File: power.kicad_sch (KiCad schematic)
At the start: 67 parts, among them J5 S7B-XH-A

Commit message: feat: change B+/P+ to B.Cu and onto one pad
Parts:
- removed PAD2: pad, MyFootLib:INPUT_PAD, symbol MyySym:PAD
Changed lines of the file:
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@@
 	)
 	(junction
-		(at 172.72 24.13)
-		(diameter 0)
-		(color 0 0 0 0)
-	)
-	(junction
 		(at 241.3 29.21)
 		(diameter 0)
@@
 	(wire
 		(pts
-			(xy 172.72 24.13) (xy 185.42 24.13)
-		)
-		(stroke
-			(width 0)
-			(type default)
-		)
-	)
-	(wire
-		(pts
 			(xy 60.96 144.78) (xy 67.31 144.78)
 		)
@@
 	(wire
 		(pts
-			(xy 160.02 24.13) (xy 172.72 24.13)
+			(xy 160.02 24.13) (xy 185.42 24.13)
 		)
 		(stroke
@@
 					(unit 1)
 				)
-			)
-		)
-	)
-	(symbol
-		(lib_id "MyySym:PAD")
-		(at 172.72 24.13 0)
-		(unit 1)
-		(body_style 1)
-		(exclude_from_sim no)
-		(in_bom yes)
-		(on_board yes)
-		(in_pos_files yes)
-		(dnp no)
-		(fields_autoplaced yes)
-		(property "Reference" "PAD2"
-			(at 175.26 22.8599 0)
-			(show_name no)
-			(do_not_autoplace no)
-			(effects
-				(font
-					(size 1.27 1.27)
-				)
-				(justify left)
-			)
-		)
-		(property "Value" "pad"
-			(at 175.26 25.3999 0)
-			(show_name no)
-			(do_not_autoplace no)
-			(effects
-				(font
-					(size 1.27 1.27)
-				)
-				(justify left)
-			)
-		)
-		(property "Footprint" "MyFootLib:INPUT_PAD"
-			(at 177.8 24.13 0)
-			(hide yes)
-			(show_name no)
-			(do_not_autoplace no)
-			(effects
-				(font
-					(size 1.27 1.27)
-				)
-			)
-		)
-		(property "Datasheet" "~"
-			(at 177.8 24.13 0)
-			(hide yes)
-			(show_name no)
-			(do_not_autoplace no)
-			(effects
-				(font
-					(size 1.27 1.27)
-				)
-			)
-		)
-		(property "Description" "PAD"
-			(at 172.72 26.162 0)
-			(hide yes)
-			(show_name no)
-			(do_not_autoplace no)
-			(effects
-				(font
-					(size 1.27 1.27)
-				)
-			)
-		)
-		(pin "1"
-		)
-		(instances
-			(project "stm32f446re-mc33772c"
-				(path "/7455d46c-434c-42dd-9f3f-f89cdb6d3cc2"
-					(reference "PAD2")
-					(unit 1)
-				)

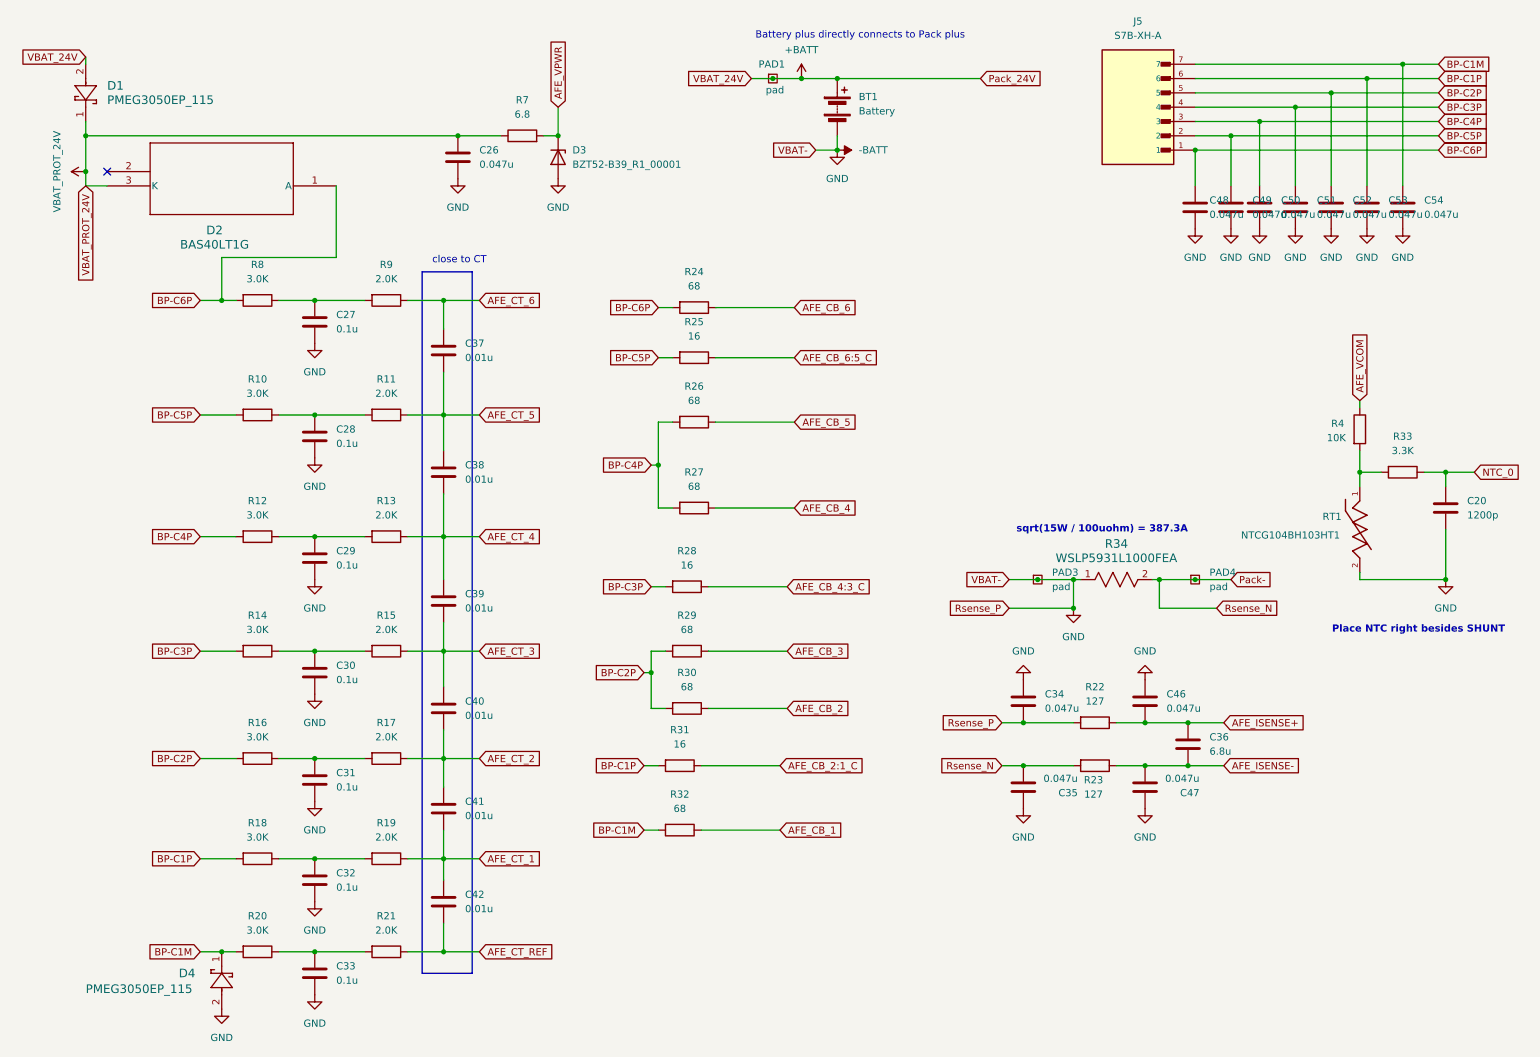
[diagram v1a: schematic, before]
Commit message: add LCPC Part #
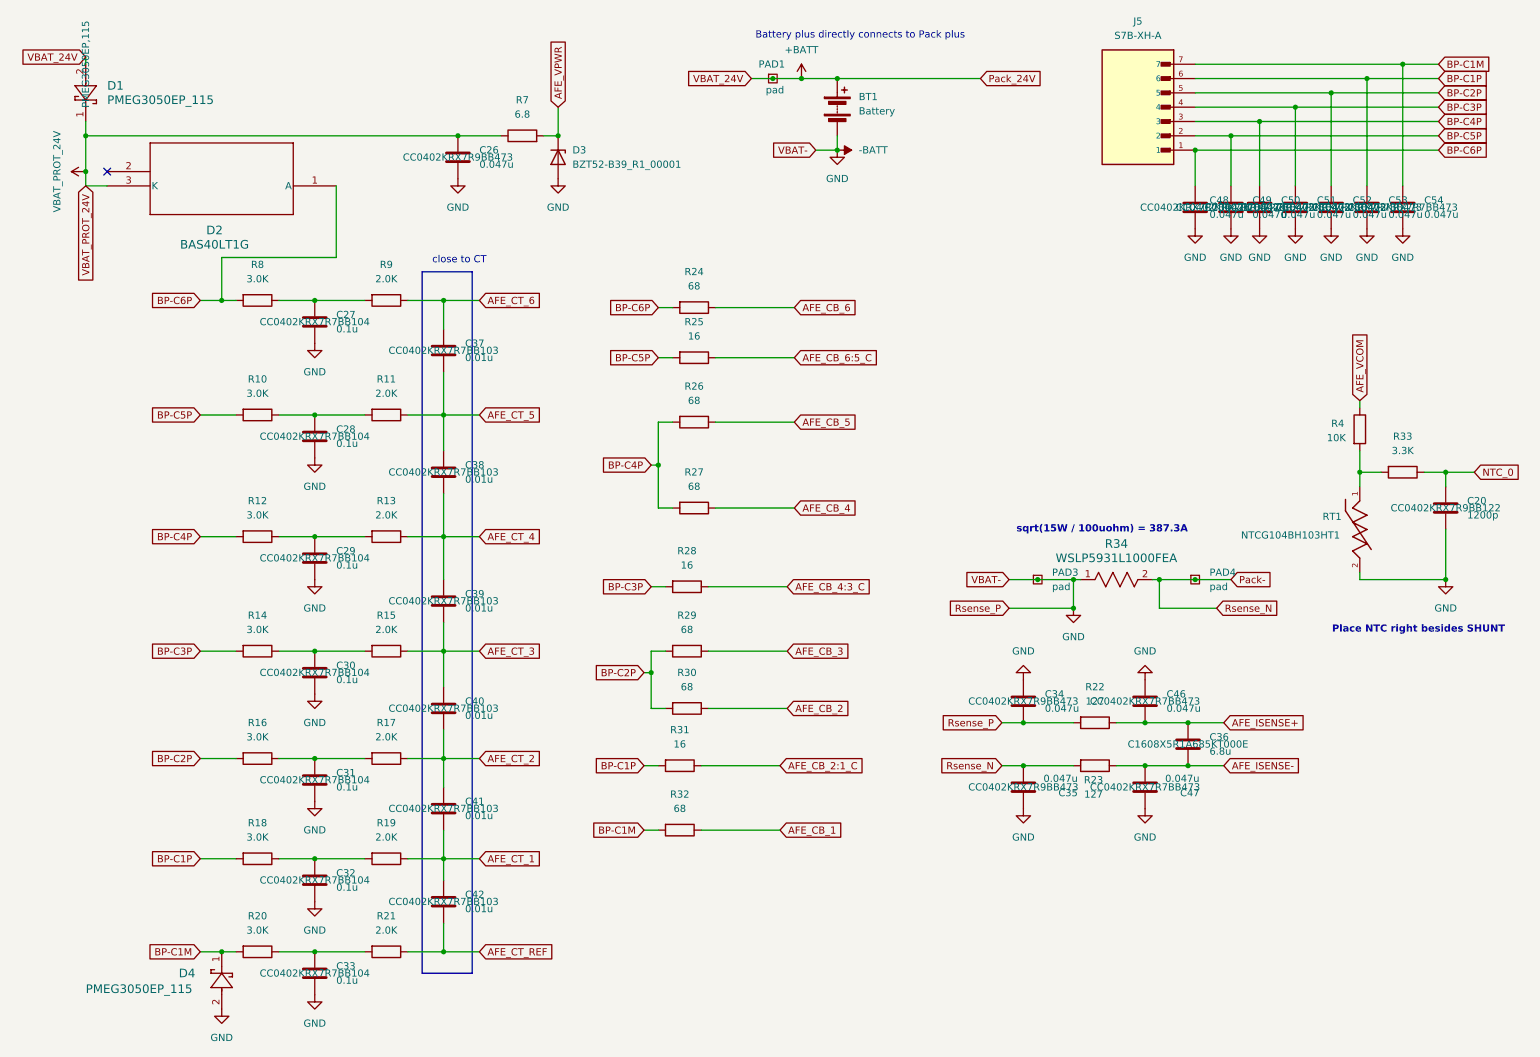
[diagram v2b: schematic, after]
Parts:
- C20: LCSC Part # (none) -> CC0402KRX7R9BB122
- C26, C34, C35: LCSC Part # (none) -> CC0402KRX7R9BB473
- C27, C28, C29, C30, C31, C32, C33: LCSC Part # (none) -> CC0402KRX7R7BB104
- C36: LCSC Part # (none) -> C1608X5R1A685KT000E
- C37, C38, C39, C40, C41, C42: LCSC Part # (none) -> CC0402KRX7R7BB103
- C46, C47, C48, C49, C50, C51, C52, C53, C54: LCSC Part # (none) -> CC0402KRX7R7BB473
- D1: LCSC Part # (none) -> PMEG3050EP,115

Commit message: update for JLCPCB with LCSC part #
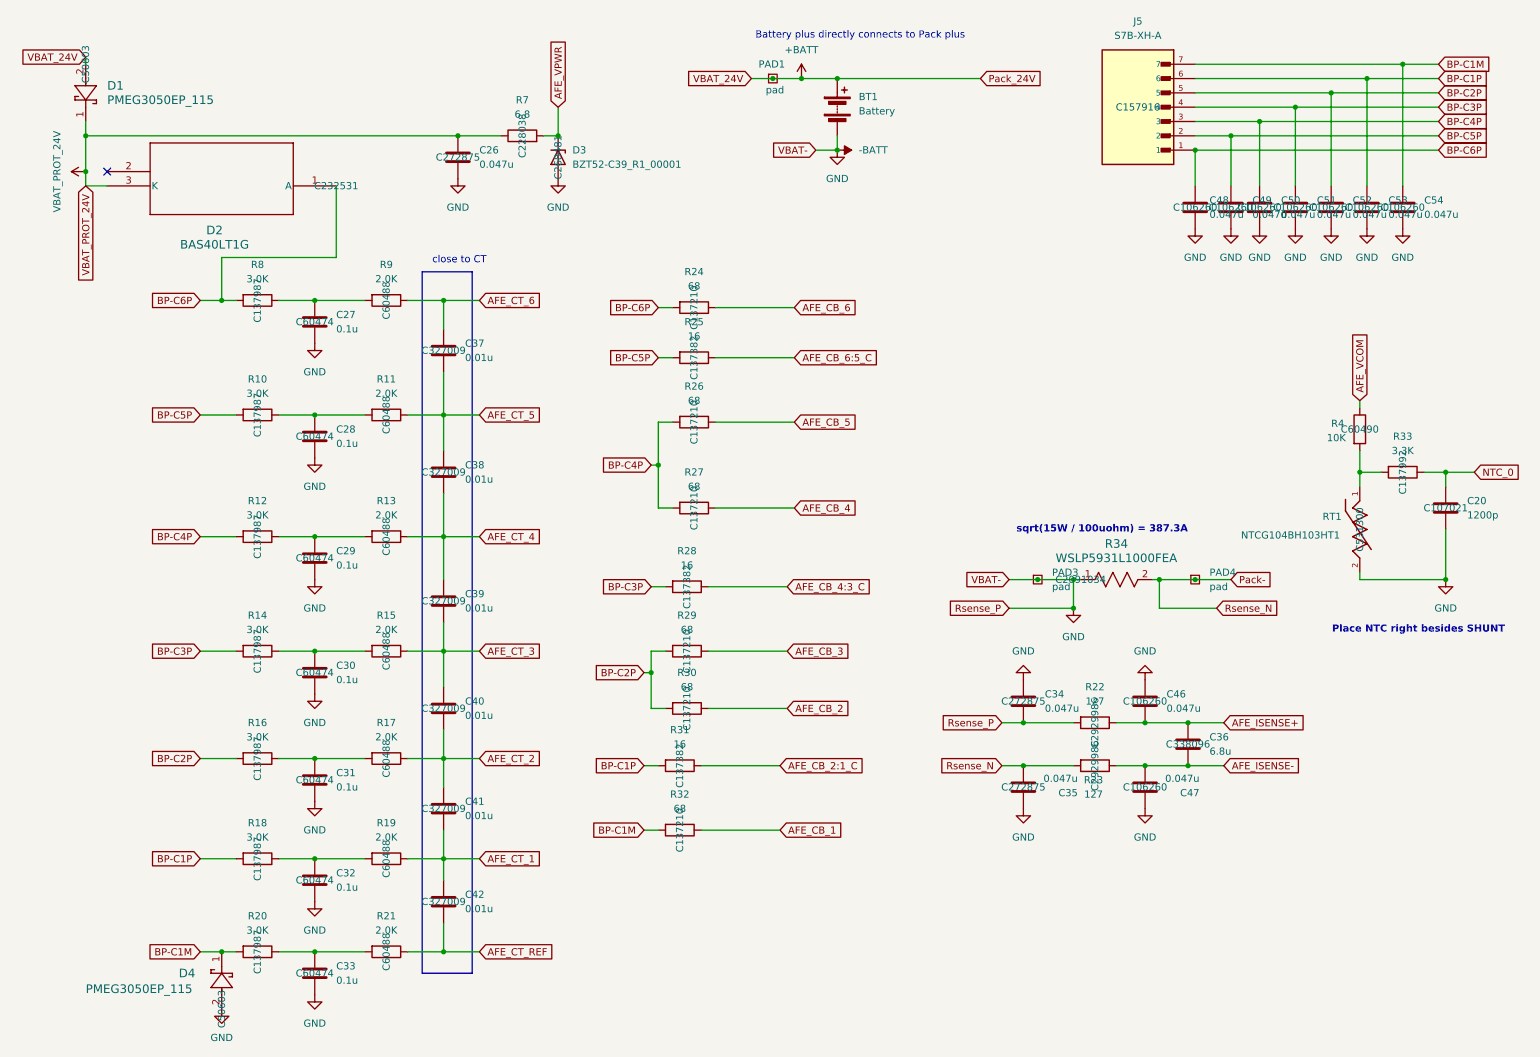
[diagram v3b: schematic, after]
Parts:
- C20: LCSC Part # CC0402KRX7R9BB122 -> C107021
- C26, C34, C35: LCSC Part # CC0402KRX7R9BB473 -> C272875
- C27, C28, C29, C30, C31, C32, C33: LCSC Part # CC0402KRX7R7BB104 -> C60474
- C36: LCSC Part # C1608X5R1A685KT000E -> C338096
- C37, C38, C39, C40, C41, C42: LCSC Part # CC0402KRX7R7BB103 -> C327009
- C46, C47, C48, C49, C50, C51, C52, C53, C54: LCSC Part # CC0402KRX7R7BB473 -> C106260
- D1: LCSC Part # PMEG3050EP,115 -> C50603
- D2: LCSC Part # (none) -> C232531
- D3: value BZT52-B39_R1_00001 -> BZT52-C39_R1_00001; LCSC Part # (none) -> C268481
- D4: LCSC Part # (none) -> C50603
- J5: LCSC Part # (none) -> C157916
- R10, R12, R14, R16, R18, R20, R8: LCSC Part # (none) -> C137987
- R11, R13, R15, R17, R19, R21, R9: LCSC Part # (none) -> C60488
- R22, R23: LCSC Part # (none) -> C2929986
- R24, R26, R27, R29, R30, R32: LCSC Part # (none) -> C137210
- R25, R28, R31: LCSC Part # (none) -> C137382
- R33: LCSC Part # (none) -> C137992
- R34: LCSC Part # (none) -> C2091034
- R4: LCSC Part # (none) -> C60490
- R7: LCSC Part # (none) -> C228038
- RT1: LCSC Part # (none) -> C531300

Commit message: export to JLCPCB
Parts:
- C27, C28, C29, C30, C31, C32, C33: value 0.1u -> 100n
- D1, D3, D4: FT Rotation Offset (none) -> 0
- D2: FT Rotation Offset (none) -> -90
- J5: FT Rotation Offset (none) -> 180
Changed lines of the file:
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@@
 			)
 		)
+		(property "FT Rotation Offset" "0"
+			(at 50.8 189.23 90)
+			(hide yes)
+			(show_name no)
+			(do_not_autoplace no)
+			(effects
+				(font
+					(size 1.27 1.27)
+				)
+			)
+		)
 		(pin "2"
 		)
@@
 			)
 		)
-		(property "Value" "0.1u"
+		(property "Value" "100n"
 			(at 71.12 184.1499 0)
 			(show_name no)
@@
 			)
 		)
-		(property "Value" "0.1u"
+		(property "Value" "100n"
 			(at 71.12 167.6399 0)
 			(show_name no)
@@
 			)
 		)
-		(property "Value" "0.1u"
+		(property "Value" "100n"
 			(at 71.12 149.8599 0)
 			(show_name no)
@@
 			)
 		)
+		(property "FT Rotation Offset" "0"
+			(at 26.67 21.59 90)
+			(hide yes)
+			(show_name no)
+			(do_not_autoplace no)
+			(effects
+				(font
+					(size 1.27 1.27)
+				)
+			)
+		)
 		(pin "2"
 		)
@@
 			)
 		)
-		(property "Value" "0.1u"
+		(property "Value" "100n"
 			(at 71.12 88.8999 0)
 			(show_name no)
@@
 			)
 		)
+		(property "FT Rotation Offset" "-90"
+			(at 71.12 43.18 0)
+			(hide yes)
+			(show_name no)
+			(do_not_autoplace no)
+			(effects
+				(font
+					(size 1.27 1.27)
+				)
+			)
+		)
 		(pin "2"
 		)
@@
 			)
 		)
+		(property "FT Rotation Offset" "180"
+			(at 213.36 29.21 0)
+			(hide yes)
+			(show_name no)
+			(do_not_autoplace no)
+			(effects
+				(font
+					(size 1.27 1.27)
+				)
+			)
+		)
 		(pin "1"
 		)
@@
 			)
 		)
-		(property "Value" "0.1u"
+		(property "Value" "100n"
 			(at 71.12 110.4899 0)
 			(show_name no)
@@
 			)
 		)
-		(property "Value" "0.1u"
+		(property "Value" "100n"
 			(at 71.12 68.5799 0)
 			(show_name no)
@@
 			)
 		)
-		(property "Value" "0.1u"
+		(property "Value" "100n"
 			(at 71.12 130.8099 0)
 			(show_name no)
@@
 			(show_name no)
 			(do_not_autoplace no)
+			(effects
+				(font
+					(size 1.27 1.27)
+				)
+			)
+		)
+		(property "FT Rotation Offset" "0"
+			(at 110.49 38.1 90)
+			(hide yes)
+			(show_name no)
+			(do_not_autoplace no)

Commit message: for PCBWay
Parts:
- C20: MPN (none) -> CC0402KRX7R9BB122
- C26, C34, C35: MPN (none) -> CC0402KRX7R9BB473
- C27, C28, C29, C30, C31, C32, C33: MPN (none) -> CC0402KRX7R7BB104
- C36: MPN (none) -> C1608X5R1A685KT000E
- C37, C38, C39, C40, C41, C42: MPN (none) -> CC0402KRX7R7BB103
- C46, C47, C48, C49, C50, C51, C52, C53, C54: MPN (none) -> CC0402KRX7R7BB473
- D1, D4: MPN (none) -> PMEG3050EP,115
- D2: MPN (none) -> BAS40LT1G
- D3: MPN (none) -> BZT52-C39_R1_00001
- J5: MPN (none) -> S7B-XH-A(LF)(SN)
- R10, R12, R14, R16, R18, R20, R8: MPN (none) -> RC0402FR-073KL
- R11, R13, R15, R17, R19, R21, R9: MPN (none) -> RC0402FR-072KL
- R22, R23: MPN (none) -> FRC0402F1270TS
- R24, R26, R27, R29, R30, R32: MPN (none) -> RC1206FR-7W68RL
- R25, R28, R31: MPN (none) -> RC1206FR-0716RL
- R33: MPN (none) -> RC0402FR-073K3L
- R34: MPN (none) -> WSLP5931L1000FEA
- R4: MPN (none) -> RC0402FR-0710KL
- R7: MPN (none) -> AC0603FR-076R8L
- RT1: MPN (none) -> NTCG104BH103HT1
